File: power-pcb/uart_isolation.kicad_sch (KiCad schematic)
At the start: 9 parts, among them J11 Screw_Terminal_01x04, U21 ADuM1201AR, U22 SRV05-4

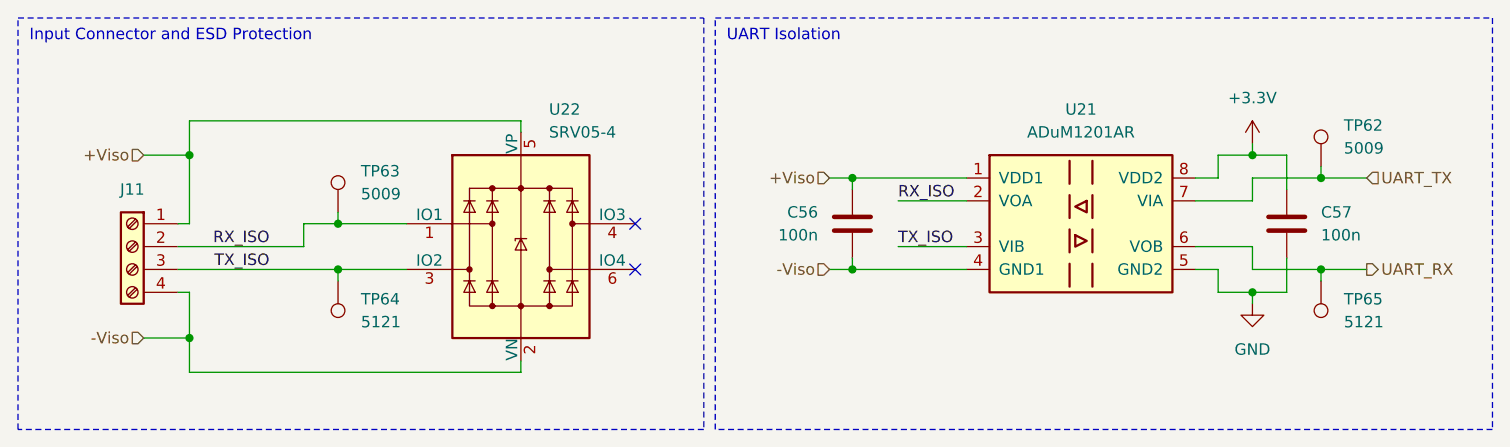
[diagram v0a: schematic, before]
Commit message: power-pcb: finish assigning JLCPCB PN
Also assigned missing footprints.
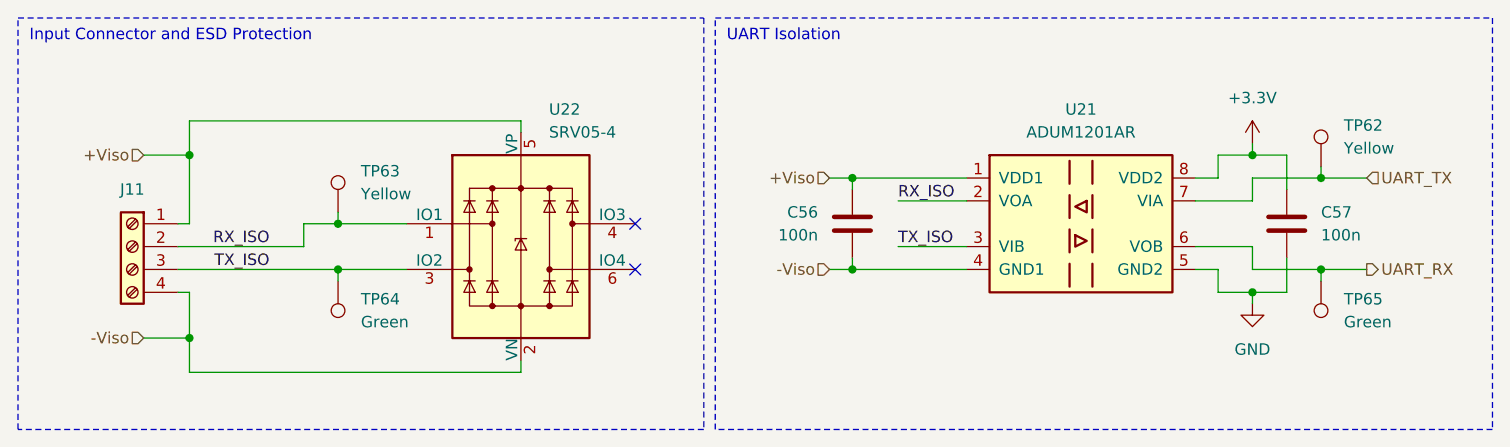
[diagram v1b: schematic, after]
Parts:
- J11: footprint (none) -> Exocet:Wuerth_Term_Blk_4pos_Side_Entry_5mm; MFR (none) -> Wuerth Eletronik; MPN (none) -> 691137710004
- TP62, TP63: value 5009 -> Yellow; footprint (none) -> TestPoint:TestPoint_Keystone_5005-5009_Compact; MFR (none) -> Keystone Electronics; MPN (none) -> 5009
- TP64, TP65: value 5121 -> Green; footprint (none) -> TestPoint:TestPoint_Keystone_5005-5009_Compact; MFR (none) -> Keystone Electronics; MPN (none) -> 5121
- U21: value ADuM1201AR -> ADUM1201AR; JLCPCB (none) -> C9669
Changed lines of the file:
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@@
 			)
 		)
-		(property "Value" "5009"
+		(property "Value" "Yellow"
 			(at 160.02 27.1779 0)
 			(show_name no)
@@
 			)
 		)
-		(property "Footprint" ""
+		(property "Footprint" "TestPoint:TestPoint_Keystone_5005-5009_Compact"
 			(at 162.56 29.21 0)
 			(hide yes)
@@
 			)
 		)
-		(property "Description" "Auxiliary Battery GND"
+		(property "Description" "Test Point"
+			(at 157.48 29.21 0)
+			(hide yes)
+			(show_name no)
+			(do_not_autoplace no)
+			(effects
+				(font
+					(size 1.27 1.27)
+				)
+			)
+		)
+		(property "MPN" "5009"
+			(at 157.48 29.21 0)
+			(hide yes)
+			(show_name no)
+			(do_not_autoplace no)
+			(effects
+				(font
+					(size 1.27 1.27)
+				)
+			)
+		)
+		(property "MFR" "Keystone Electronics"
 			(at 157.48 29.21 0)
 			(hide yes)
@@
 			)
 		)
-		(property "Value" "5121"
+		(property "Value" "Green"
 			(at 50.8 46.4819 0)
 			(show_name no)
@@
 			)
 		)
-		(property "Footprint" ""
+		(property "Footprint" "TestPoint:TestPoint_Keystone_5005-5009_Compact"
 			(at 43.18 41.91 0)
 			(hide yes)
@@
 			)
 		)
-		(property "Description" "Auxiliary Battery GND"
+		(property "Description" "Test Point"
+			(at 48.26 41.91 0)
+			(hide yes)
+			(show_name no)
+			(do_not_autoplace no)
+			(effects
+				(font
+					(size 1.27 1.27)
+				)
+			)
+		)
+		(property "MPN" "5121"
+			(at 48.26 41.91 0)
+			(hide yes)
+			(show_name no)
+			(do_not_autoplace no)
+			(effects
+				(font
+					(size 1.27 1.27)
+				)
+			)
+		)
+		(property "MFR" "Keystone Electronics"
 			(at 48.26 41.91 0)
 			(hide yes)
@@
 			)
 		)
-		(property "Value" "5009"
+		(property "Value" "Yellow"
 			(at 50.8 32.2579 0)
 			(show_name no)
@@
 			)
 		)
-		(property "Footprint" ""
+		(property "Footprint" "TestPoint:TestPoint_Keystone_5005-5009_Compact"
 			(at 53.34 34.29 0)
 			(hide yes)
@@
 			)
 		)
-		(property "Description" "Auxiliary Battery GND"
+		(property "Description" "Test Point"
+			(at 48.26 34.29 0)
+			(hide yes)
+			(show_name no)
+			(do_not_autoplace no)
+			(effects
+				(font
+					(size 1.27 1.27)
+				)
+			)
+		)
+		(property "MPN" "5009"
+			(at 48.26 34.29 0)
+			(hide yes)
+			(show_name no)
+			(do_not_autoplace no)
+			(effects
+				(font
+					(size 1.27 1.27)
+				)
+			)
+		)
+		(property "MFR" "Keystone Electronics"
 			(at 48.26 34.29 0)
 			(hide yes)
@@
 			)
 		)
-		(property "Footprint" ""
+		(property "Footprint" "Exocet:Wuerth_Term_Blk_4pos_Side_Entry_5mm"
 			(at 25.4 38.1 0)
 			(hide yes)
@@
 		)
 		(property "Description" "Generic screw terminal, single row, 01x04, script generated (kicad-library-utils/schlib/autogen/connector/)"
+			(at 25.4 38.1 0)
+			(hide yes)
+			(show_name no)
+			(do_not_autoplace no)
+			(effects
+				(font
+					(size 1.27 1.27)
+				)
+			)
+		)
+		(property "MFR" "Wuerth Eletronik"
+			(at 25.4 38.1 0)
+			(hide yes)
+			(show_name no)
+			(do_not_autoplace no)
+			(effects
+				(font
+					(size 1.27 1.27)
+				)
+			)
+		)
+		(property "MPN" "691137710004"
 			(at 25.4 38.1 0)
 			(hide yes)
@@
 			)
 		)
-		(property "Value" "5121"
+		(property "Value" "Green"
 			(at 160.02 46.4819 0)
 			(show_name no)
@@
 			)
 		)
-		(property "Footprint" ""
+		(property "Footprint" "TestPoint:TestPoint_Keystone_5005-5009_Compact"
 			(at 152.4 41.91 0)
 			(hide yes)
@@
 			)
 		)
-		(property "Description" "Auxiliary Battery GND"
+		(property "Description" "Test Point"
+			(at 157.48 41.91 0)
+			(hide yes)
+			(show_name no)
+			(do_not_autoplace no)
+			(effects
+				(font
+					(size 1.27 1.27)
+				)
+			)
+		)
+		(property "MPN" "5121"
+			(at 157.48 41.91 0)
+			(hide yes)
+			(show_name no)
+			(do_not_autoplace no)
+			(effects
+				(font
+					(size 1.27 1.27)
+				)
+			)
+		)
+		(property "MFR" "Keystone Electronics"
 			(at 157.48 41.91 0)
 			(hide yes)
@@
 			)
 		)
-		(property "Value" "ADuM1201AR"
+		(property "Value" "ADUM1201AR"
 			(at 130.81 25.4 0)
 			(show_name no)
@@
 			(at 130.81 35.56 0)
 			(hide yes)
+			(show_name no)
+			(do_not_autoplace no)
+			(effects
+				(font
+					(size 1.27 1.27)
+				)
+			)
+		)
+		(property "JLCPCB" "C9669"
+			(at 130.81 35.56 0)
+			(hide yes)
